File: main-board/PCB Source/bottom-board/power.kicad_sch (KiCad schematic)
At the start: 25 parts, among them P3 BARREL_JACK, U1 TS2596, U2 TL750M10CKVURG3, U9 LD1117S50TR

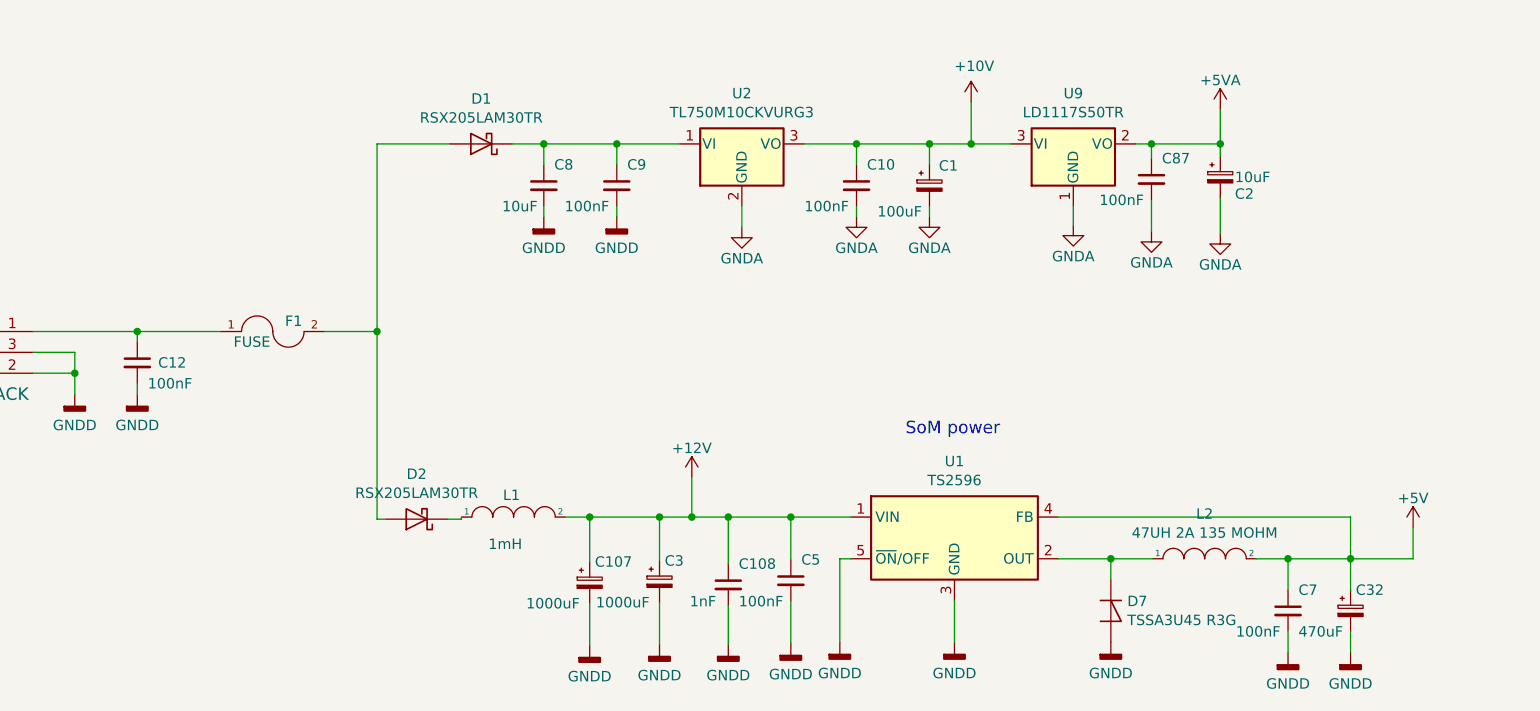
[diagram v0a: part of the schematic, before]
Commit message: mainboard: add bias buffer, update MPNs, clean schematic
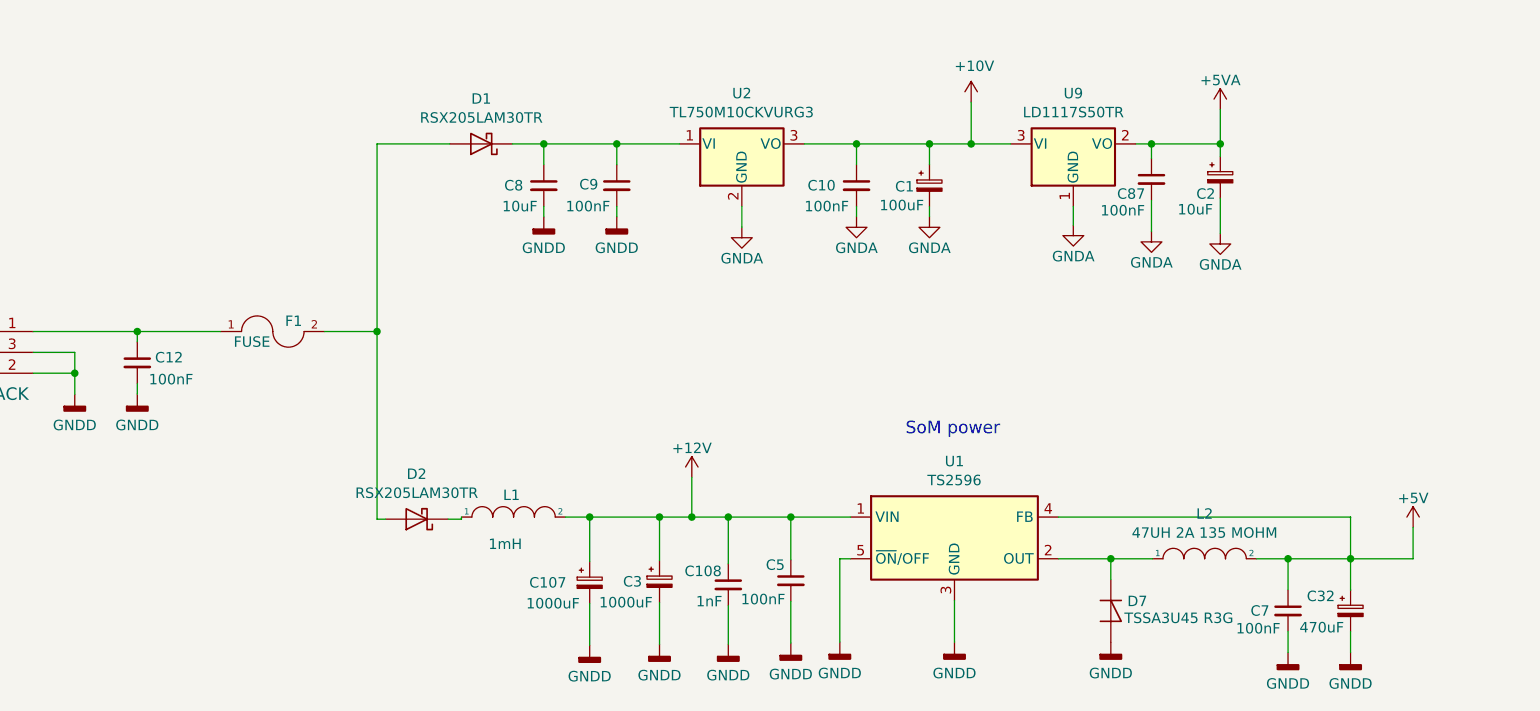
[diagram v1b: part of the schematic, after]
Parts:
- C108: MPN C0603X7R500-103KNP -> C0603X7R500-102KNP
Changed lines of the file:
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@@
     (title "MOD Dwarf - Main Board")
     (date "2021-09-06")
-    (rev "1.3")
+    (rev "3.0")
     (company "MOD Devices GmbH")
     (comment 1 "Dwarf Audio processing board")
@@
   (symbol (lib_id "bottom-board-rescue:C_Small") (at 107.696 97.155 0) (unit 1)
     (in_bom yes) (on_board yes)
-    (property "Reference" "C9" (id 0) (at 108.966 94.615 0)
-      (effects (font (size 1.27 1.27)) (justify left))
-    )
-    (property "Value" "100nF" (id 1) (at 101.346 99.695 0)
+    (property "Reference" "C9" (id 0) (at 103.124 97.028 0)
+      (effects (font (size 1.27 1.27)) (justify left))
+    )
+    (property "Value" "100nF" (id 1) (at 101.473 99.695 0)
       (effects (font (size 1.27 1.27)) (justify left))
     )
@@
   (symbol (lib_id "bottom-board-rescue:C_Small") (at 136.906 97.155 0) (unit 1)
     (in_bom yes) (on_board yes)
-    (property "Reference" "C10" (id 0) (at 138.176 94.615 0)
+    (property "Reference" "C10" (id 0) (at 130.937 97.155 0)
       (effects (font (size 1.27 1.27)) (justify left))
     )
@@
   (symbol (lib_id "bottom-board-rescue:C_Small-Device") (at 98.806 97.155 0) (unit 1)
     (in_bom yes) (on_board yes)
-    (property "Reference" "C8" (id 0) (at 100.076 94.615 0)
+    (property "Reference" "C8" (id 0) (at 93.98 97.155 0)
       (effects (font (size 1.27 1.27)) (justify left))
     )
@@
   (symbol (lib_id "bottom-board-rescue:C_Small") (at 128.905 145.288 0) (unit 1)
     (in_bom yes) (on_board yes)
-    (property "Reference" "C5" (id 0) (at 130.175 142.748 0)
-      (effects (font (size 1.27 1.27)) (justify left))
-    )
-    (property "Value" "100nF" (id 1) (at 122.555 147.828 0)
+    (property "Reference" "C5" (id 0) (at 125.857 143.383 0)
+      (effects (font (size 1.27 1.27)) (justify left))
+    )
+    (property "Value" "100nF" (id 1) (at 122.809 147.574 0)
       (effects (font (size 1.27 1.27)) (justify left))
     )
@@
       (effects (font (size 1.27 1.27)) (justify left))
     )
-    (property "Value" "TSSA3U45 R3G" (id 1) (at 169.9006 150.114 90)
+    (property "Value" "TSSA3U45 R3G" (id 1) (at 169.545 149.86 90)
       (effects (font (size 1.27 1.27)) (justify left))
     )
@@
   (symbol (lib_id "bottom-board-rescue:C_Small") (at 189.484 148.971 0) (unit 1)
     (in_bom yes) (on_board yes)
-    (property "Reference" "C7" (id 0) (at 190.754 146.431 0)
-      (effects (font (size 1.27 1.27)) (justify left))
-    )
-    (property "Value" "100nF" (id 1) (at 183.134 151.511 0)
+    (property "Reference" "C7" (id 0) (at 184.912 148.971 0)
+      (effects (font (size 1.27 1.27)) (justify left))
+    )
+    (property "Value" "100nF" (id 1) (at 183.134 151.13 0)
       (effects (font (size 1.27 1.27)) (justify left))
     )
@@
   (symbol (lib_id "bottom-board-rescue:CP_Small") (at 112.903 145.415 0) (unit 1)
     (in_bom yes) (on_board yes)
-    (property "Reference" "C3" (id 0) (at 113.538 142.875 0)
-      (effects (font (size 1.27 1.27)) (justify left))
-    )
-    (property "Value" "1000uF" (id 1) (at 105.156 147.955 0)
+    (property "Reference" "C3" (id 0) (at 108.458 145.415 0)
+      (effects (font (size 1.27 1.27)) (justify left))
+    )
+    (property "Value" "1000uF" (id 1) (at 105.537 147.955 0)
       (effects (font (size 1.27 1.27)) (justify left))
     )
@@
   (symbol (lib_id "bottom-board-rescue:CP_Small") (at 197.104 148.971 0) (unit 1)
     (in_bom yes) (on_board yes)
-    (property "Reference" "C32" (id 0) (at 197.739 146.431 0)
-      (effects (font (size 1.27 1.27)) (justify left))
-    )
-    (property "Value" "470uF" (id 1) (at 190.754 151.511 0)
+    (property "Reference" "C32" (id 0) (at 191.77 147.193 0)
+      (effects (font (size 1.27 1.27)) (justify left))
+    )
+    (property "Value" "470uF" (id 1) (at 190.881 151.003 0)
       (effects (font (size 1.27 1.27)) (justify left))
     )
@@
   (symbol (lib_id "bottom-board-rescue:C_Small") (at 49.276 118.745 0) (unit 1)
     (in_bom yes) (on_board yes)
-    (property "Reference" "C12" (id 0) (at 51.816 118.745 0)
-      (effects (font (size 1.27 1.27)) (justify left))
-    )
-    (property "Value" "100nF" (id 1) (at 50.546 121.285 0)
+    (property "Reference" "C12" (id 0) (at 51.435 118.11 0)
+      (effects (font (size 1.27 1.27)) (justify left))
+    )
+    (property "Value" "100nF" (id 1) (at 50.673 120.777 0)
       (effects (font (size 1.27 1.27)) (justify left))
     )
@@
   (symbol (lib_id "bottom-board-rescue:CP_Small") (at 181.229 96.139 0) (unit 1)
     (in_bom yes) (on_board yes)
-    (property "Reference" "C2" (id 0) (at 183.007 98.171 0)
-      (effects (font (size 1.27 1.27)) (justify left))
-    )
-    (property "Value" "10uF" (id 1) (at 183.007 96.139 0)
+    (property "Reference" "C2" (id 0) (at 178.308 98.171 0)
+      (effects (font (size 1.27 1.27)) (justify left))
+    )
+    (property "Value" "10uF" (id 1) (at 176.022 100.076 0)
       (effects (font (size 1.27 1.27)) (justify left))
     )
@@
   (symbol (lib_id "bottom-board-rescue:C_Small") (at 172.847 96.393 0) (unit 1)
     (in_bom yes) (on_board yes)
-    (property "Reference" "C87" (id 0) (at 174.117 93.853 0)
-      (effects (font (size 1.27 1.27)) (justify left))
-    )
-    (property "Value" "100nF" (id 1) (at 166.497 98.933 0)
+    (property "Reference" "C87" (id 0) (at 168.656 98.171 0)
+      (effects (font (size 1.27 1.27)) (justify left))
+    )
+    (property "Value" "100nF" (id 1) (at 166.624 100.203 0)
       (effects (font (size 1.27 1.27)) (justify left))
     )
@@
   (symbol (lib_id "bottom-board-rescue:CP_Small") (at 145.796 97.155 0) (unit 1)
     (in_bom yes) (on_board yes)
-    (property "Reference" "C1" (id 0) (at 146.939 94.742 0)
-      (effects (font (size 1.27 1.27)) (justify left))
-    )
-    (property "Value" "100uF" (id 1) (at 139.446 100.33 0)
+    (property "Reference" "C1" (id 0) (at 141.605 97.282 0)
+      (effects (font (size 1.27 1.27)) (justify left))
+    )
+    (property "Value" "100uF" (id 1) (at 139.7 99.568 0)
       (effects (font (size 1.27 1.27)) (justify left))
     )
@@
   (symbol (lib_id "bottom-board-rescue:CP_Small") (at 104.394 145.542 0) (unit 1)
     (in_bom yes) (on_board yes)
-    (property "Reference" "C107" (id 0) (at 105.029 143.002 0)
+    (property "Reference" "C107" (id 0) (at 97.028 145.542 0)
       (effects (font (size 1.27 1.27)) (justify left))
     )
@@
   (symbol (lib_id "bottom-board-rescue:C_Small") (at 121.285 145.796 0) (unit 1)
     (in_bom yes) (on_board yes)
-    (property "Reference" "C108" (id 0) (at 122.555 143.256 0)
-      (effects (font (size 1.27 1.27)) (justify left))
-    )
-    (property "Value" "1nF" (id 1) (at 116.586 147.828 0)
+    (property "Reference" "C108" (id 0) (at 115.951 144.145 0)
+      (effects (font (size 1.27 1.27)) (justify left))
+    )
+    (property "Value" "1nF" (id 1) (at 117.348 147.828 0)
       (effects (font (size 1.27 1.27)) (justify left))
     )
@@
       (effects (font (size 1.524 1.524)))
     )
-    (property "MPN" "C0603X7R500-103KNP" (id 4) (at -19.685 216.916 0)
-      (effects (font (size 1.27 1.27)) hide)
-    )
+    (property "MPN" "C0603X7R500-102KNP" (id 4) (at -19.685 216.916 0)
+      (effects (font (size 1.27 1.27)) hide)
+    )
